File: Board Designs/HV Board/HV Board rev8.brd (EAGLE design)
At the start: 147.4 x 71.4 mm, 65 parts, among them IC1 OKI-78SR, IC2 NE5532SOIC

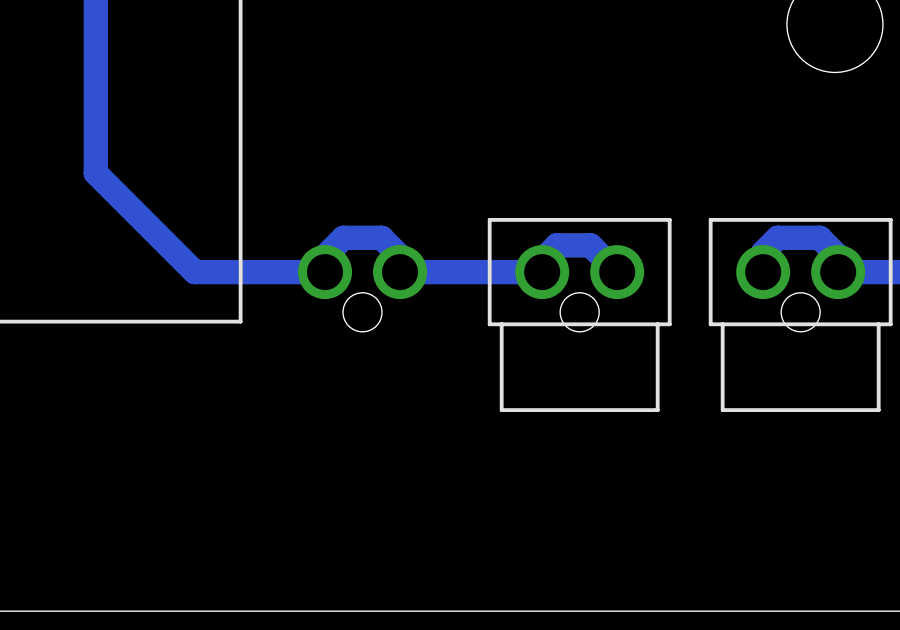
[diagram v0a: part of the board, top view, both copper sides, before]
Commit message: Prep silkscreen and dimensions for manufacture
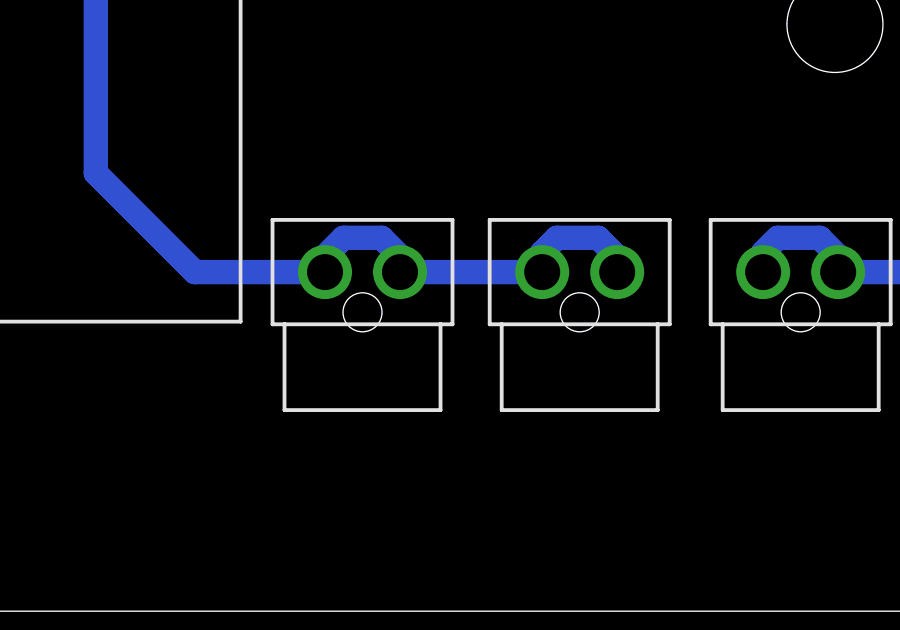
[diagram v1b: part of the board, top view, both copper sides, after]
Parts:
- flipped HV+FUSED_1A to the top
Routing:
- net HV+FUSED_1A: track 29.0 -> 29.7 mm

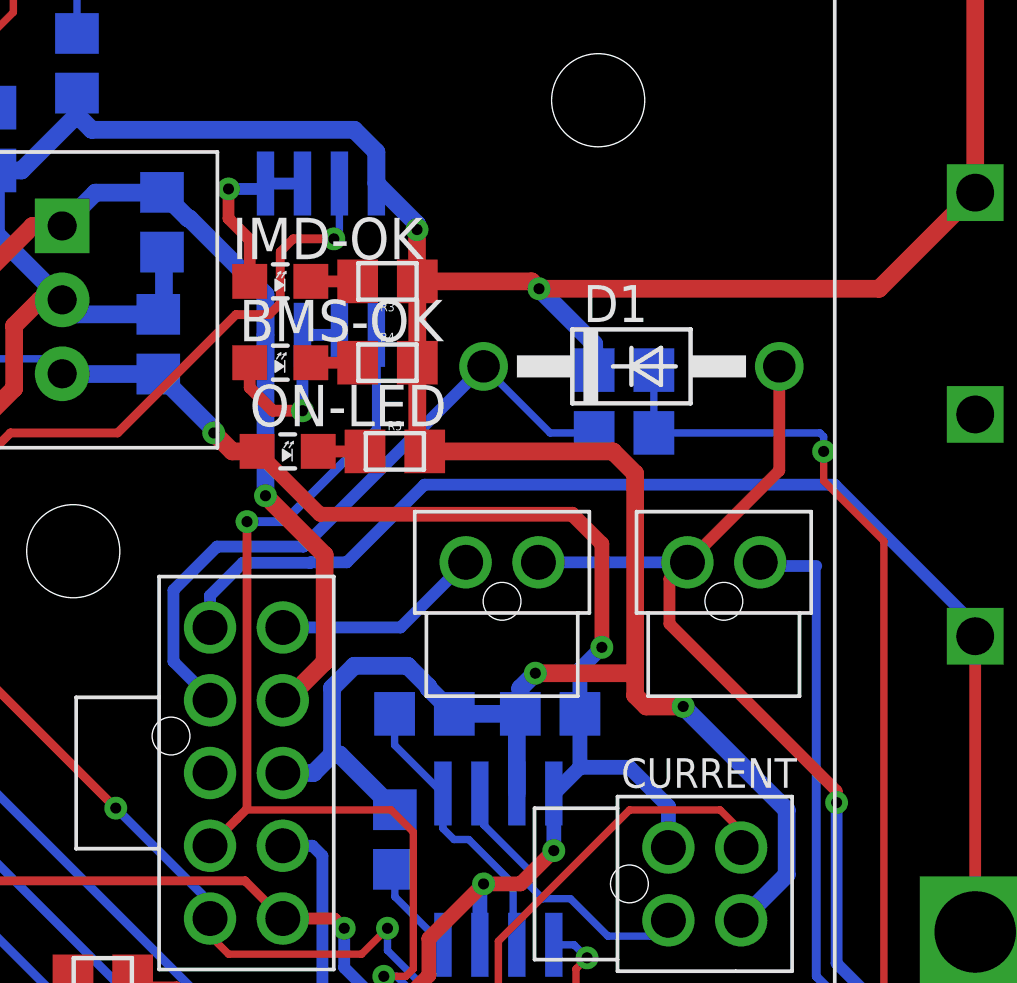
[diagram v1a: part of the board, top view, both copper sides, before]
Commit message: Silkscreen modifications, small adjustments to trace locations
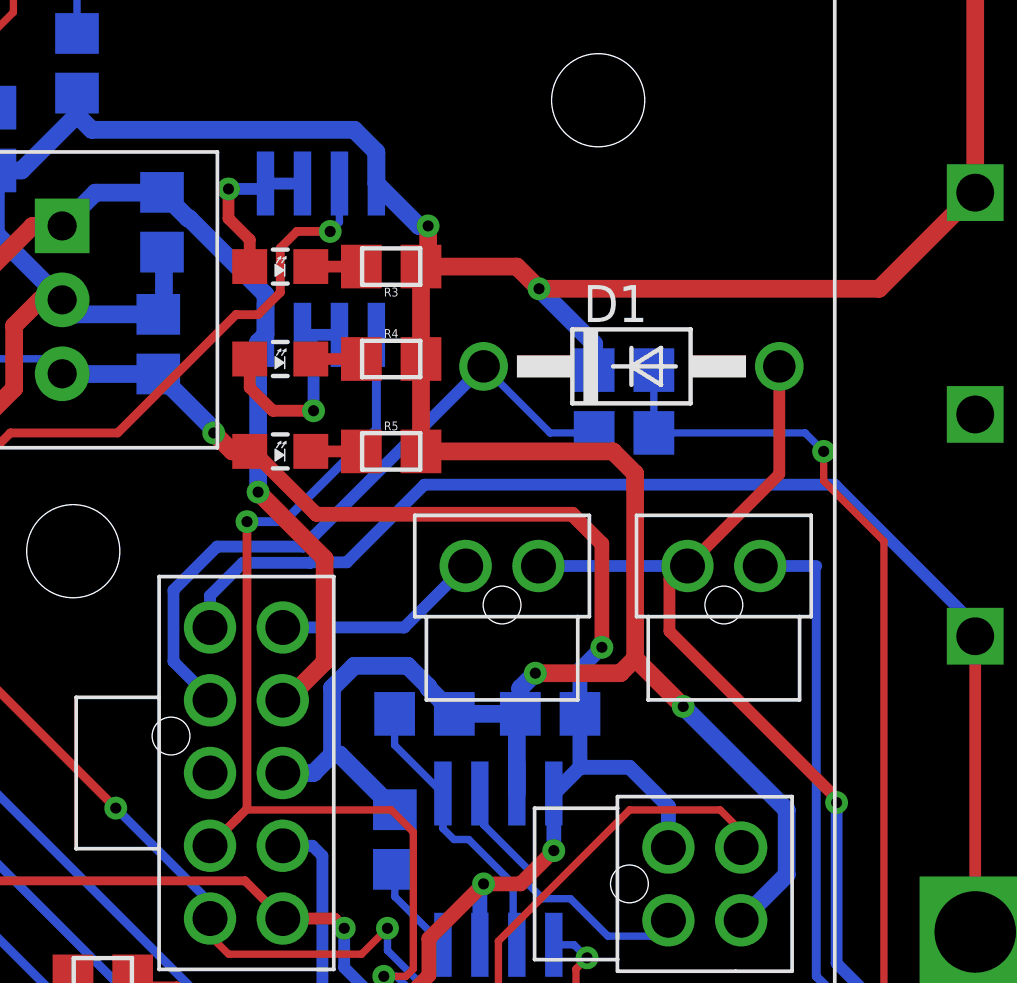
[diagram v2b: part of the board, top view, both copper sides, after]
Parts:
- moved R3 0.52 mm to (25.4, 45.2)
- moved IMD-OK 0.51 mm to (21.6, 45.2)
- moved ON-LED 0.25 mm to (21.6, 38.9)
- moved R4 0.18 mm to (25.4, 42.0)
- moved BMS-OK 0.13 mm to (21.6, 42.0)
- moved INTERLOCK 0.13 mm to (29.2, 34.9)
- moved R5 0.13 mm to (25.4, 38.9)
- moved RELAYS 0.13 mm to (36.8, 34.9)
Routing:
- net N$43: track 6.87 -> 7.54 mm
- net N$42: track 6.09 -> 5.59 mm
